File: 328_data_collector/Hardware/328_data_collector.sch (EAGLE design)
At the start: 28 parts, among them Q1 8/16/20MHz, U1 ATMEGA328, U2 MIC5205

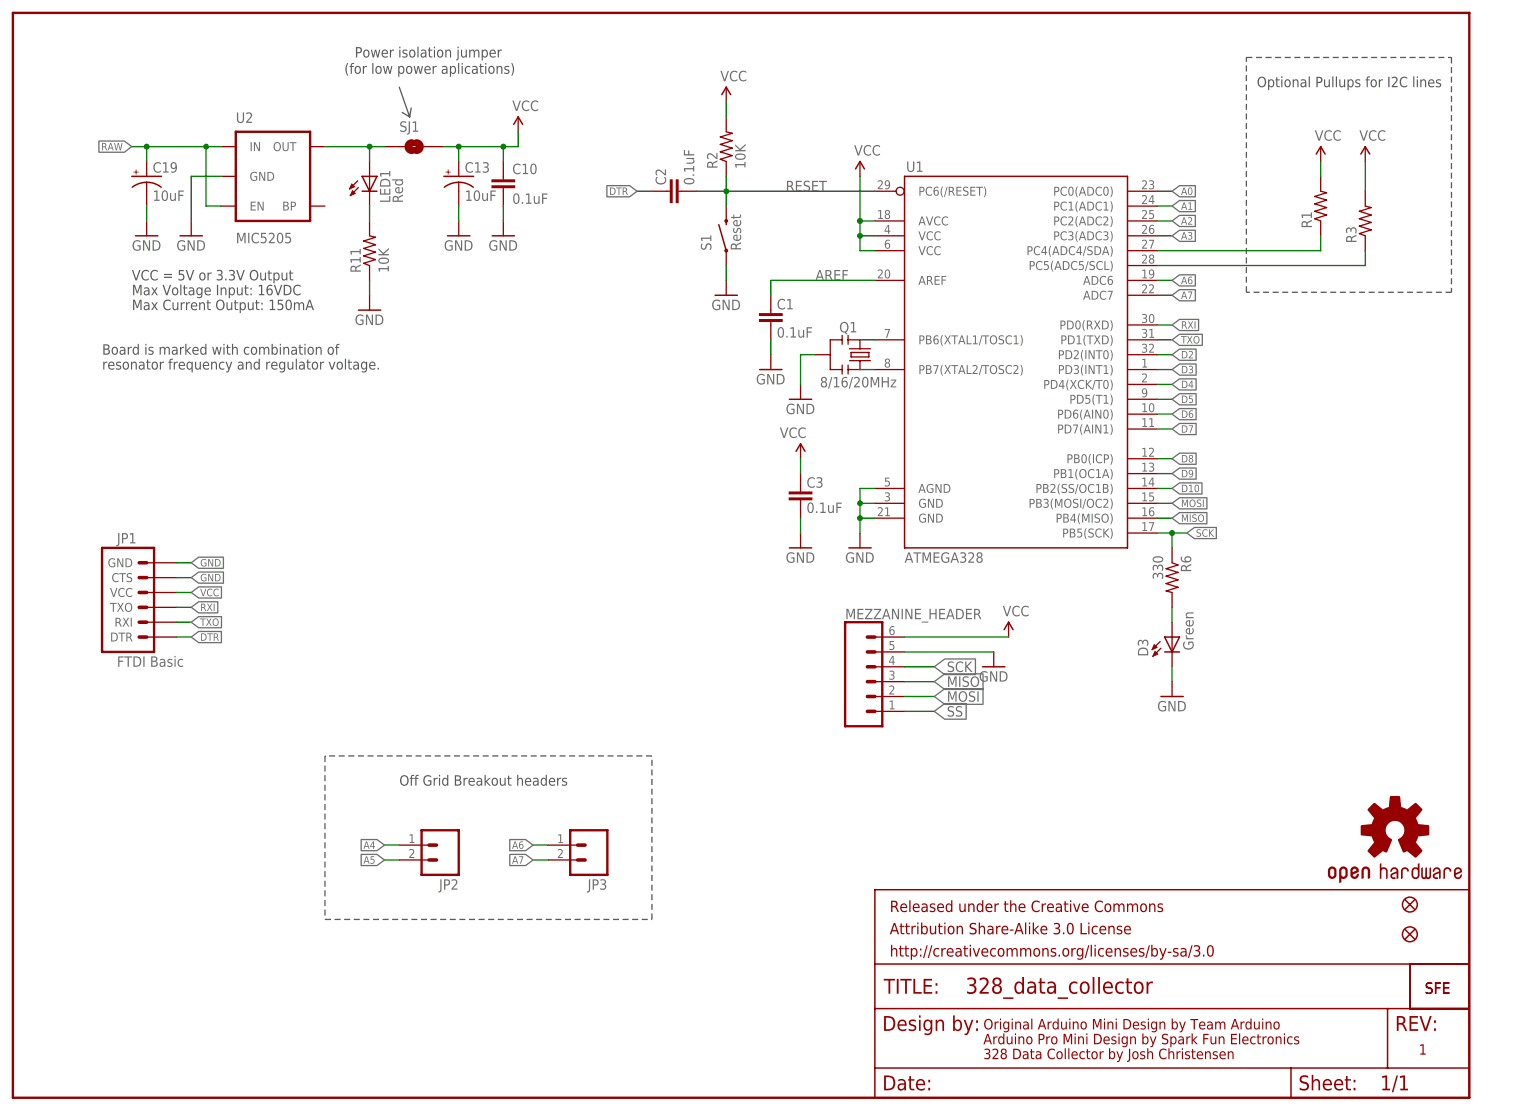
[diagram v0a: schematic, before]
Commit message: More work on 328 schematic. Culled regulator. Left decoupling caps, pretty sure they're overkill though. Consult Brandon and Kirby.
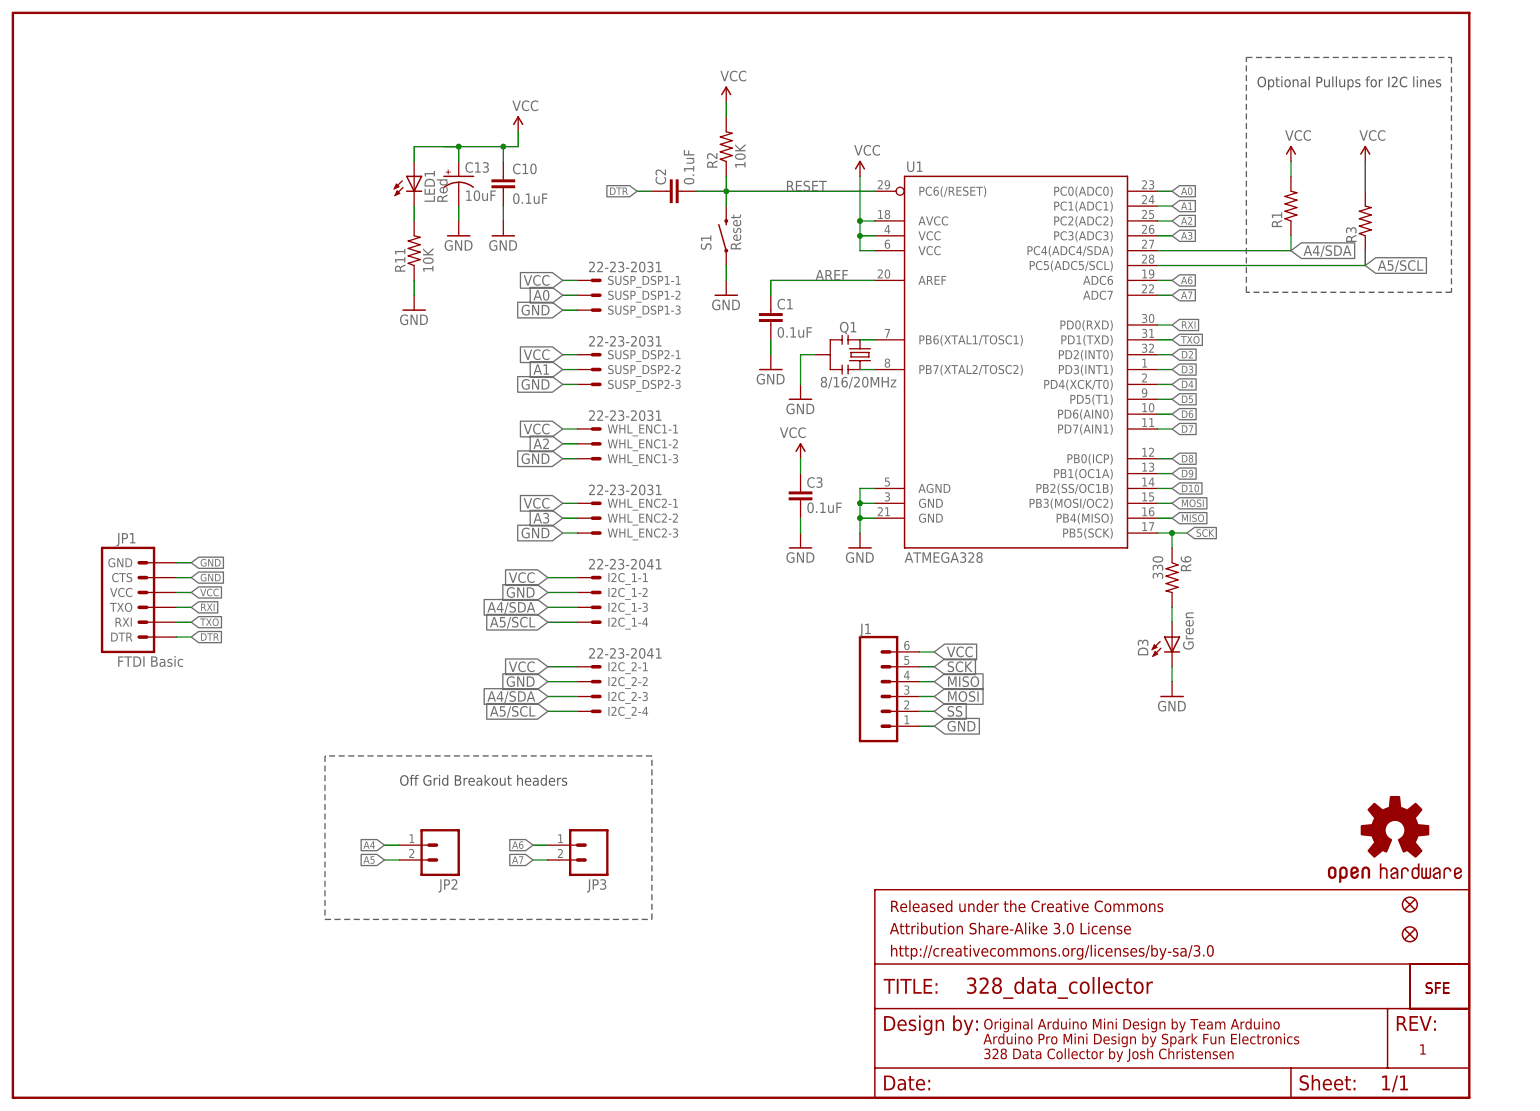
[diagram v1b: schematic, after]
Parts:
- removed C19: 10uF, SparkFun:CAP_POL1206
- removed MEZZANINE_HEADER: (no value), SparkFun-Connectors:CONN_06SILK_FEMALE_PTH
- removed SJ1: SOLDERJUMPERNC, SparkFun-Passives:SOLDERJUMPERNC
- removed U2: MIC5205, SparkFun:V_REG_LDOSMD
- added I2C_1, I2C_2: 22-23-2041, con-molex:22-23-2041
- added J1: (no value), SparkFun-Connectors:CONN_06SILK_FEMALE_PTH
- added SUSP_DSP1, SUSP_DSP2, WHL_ENC1, WHL_ENC2: 22-23-2031, con-molex:22-23-2031
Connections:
- removed net 3.3V: MEZZANINE_HEADER.6
- removed net N$3: LED1.A, SJ1.1, U2.OUT
- removed net RAW: C19.+, U2.EN, U2.IN
- new net A4/SDA: I2C_1-3.S, I2C_2-3.S, R1.1, U1.PC4(ADC4/SDA)
- new net A5/SCL: I2C_1-4.S, I2C_2-4.S, R3.1, U1.PC5(ADC5/SCL)
- net A0: now also SUSP_DSP1-2.S
- net A1: now also SUSP_DSP2-2.S
- net A2: now also WHL_ENC1-2.S
- net A3: now also WHL_ENC2-2.S
- net A4: no longer R1.1, U1.PC4(ADC4/SDA)
- net A5: no longer R3.1, U1.PC5(ADC5/SCL)
- net GND: now also I2C_1-2.S, I2C_2-2.S, J1.1, SUSP_DSP1-3.S, SUSP_DSP2-3.S, WHL_ENC1-3.S, WHL_ENC2-3.S; no longer C19.-, MEZZANINE_HEADER.5, U2.GND
- net MISO: now also J1.4; no longer MEZZANINE_HEADER.3
- net MOSI: now also J1.3; no longer MEZZANINE_HEADER.2
- net SCK: now also J1.5; no longer MEZZANINE_HEADER.4
- net SS: now also J1.2; no longer MEZZANINE_HEADER.1
- net VCC: now also I2C_1-1.S, I2C_2-1.S, J1.6, LED1.A, SUSP_DSP1-1.S, SUSP_DSP2-1.S, WHL_ENC1-1.S, WHL_ENC2-1.S; no longer SJ1.2
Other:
- note removed: "(for low power aplications)"
- note removed: "Board is marked with combination of"
- note removed: "Max Current Output: 150mA"
- note removed: "Max Voltage Input: 16VDC"
- note removed: "Power isolation jumper"
- note removed: "VCC = 5V or 3.3V Output"
- note removed: "resonator frequency and regulator voltage."
- moved on the sheet: LED1, R1, R11
